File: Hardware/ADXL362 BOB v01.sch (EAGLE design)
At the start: 9 parts

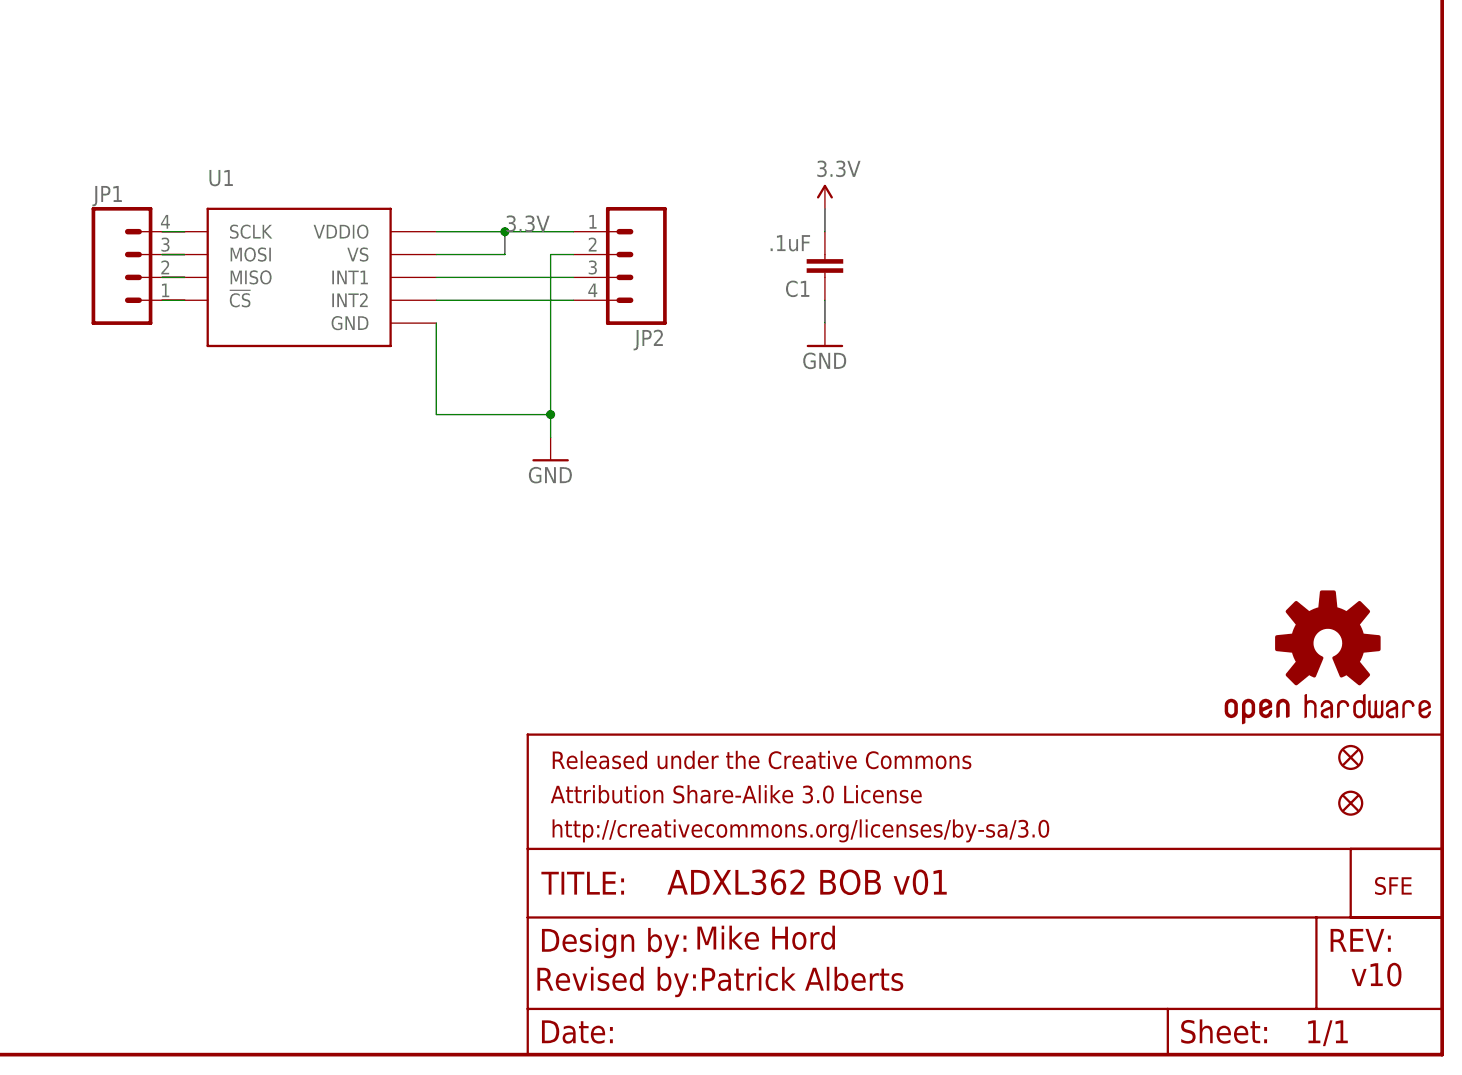
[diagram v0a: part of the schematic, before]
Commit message: Adding part info to README, adding current files to repo
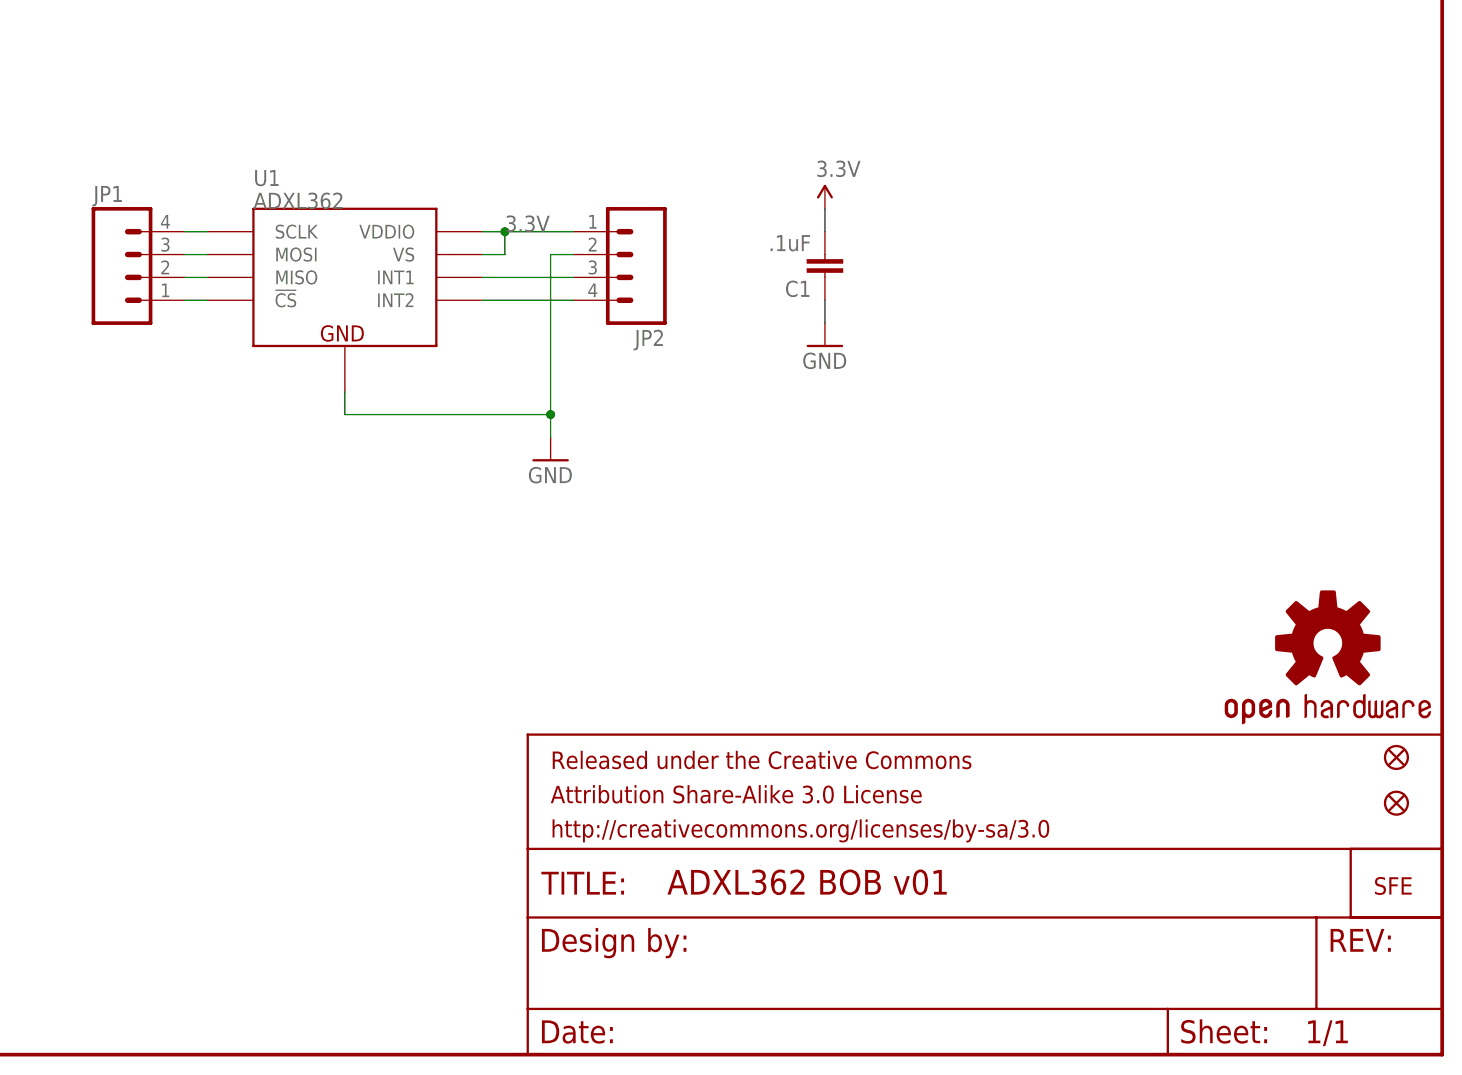
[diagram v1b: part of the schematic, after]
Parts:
- removed FID1, FID2: FIDUCIAL1X2, SparkFun-Aesthetics:FIDUCIAL1X2
- added JP4, JP5: FIDUCIALUFIDUCIAL, SparkFun:FIDUCIALUFIDUCIAL
- C1: device SparkFun-Capacitors:0.1UF-25V(+80/-20%)(0603) -> SparkFun-Passives:CAP0402-CAP
- U1: value (none) -> ADXL362; device SparkFun-Sensors:ADXL362ADXL362-1:1 -> SparkFun-Sensors:ADXL362
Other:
- note removed: "Mike Hord"
- note removed: "Revised by:Patrick Alberts"
- note removed: "v10"
- moved on the sheet: U1
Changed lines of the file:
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@@
 <?xml version="1.0" encoding="utf-8"?>
 <!DOCTYPE eagle SYSTEM "eagle.dtd">
-<eagle version="6.5.0">
+<eagle version="6.2">
 <drawing>
 <settings>
@@
 <layer number="106" name="bPlate" color="7" fill="1" visible="no" active="yes"/>
 <layer number="107" name="Crop" color="7" fill="1" visible="no" active="yes"/>
-<layer number="108" name="tplace-old" color="10" fill="1" visible="yes" active="yes"/>
-<layer number="109" name="ref-old" color="11" fill="1" visible="yes" active="yes"/>
 <layer number="116" name="Patch_BOT" color="9" fill="4" visible="no" active="yes"/>
 <layer number="121" name="_tsilk" color="7" fill="1" visible="no" active="yes"/>
@@
 <layer number="144" name="Drill_legend" color="7" fill="1" visible="no" active="yes"/>
 <layer number="151" name="HeatSink" color="7" fill="1" visible="no" active="yes"/>
-<layer number="199" name="Contour" color="7" fill="1" visible="yes" active="yes"/>
 <layer number="200" name="200bmp" color="1" fill="10" visible="no" active="yes"/>
 <layer number="201" name="201bmp" color="2" fill="10" visible="no" active="yes"/>
@@
 </classes>
 <parts>
-<part name="U1" library="SparkFun-Sensors" deviceset="ADXL362" device="ADXL362-1:1"/>
+<part name="U1" library="SparkFun-Sensors" deviceset="ADXL362" device=""/>
 <part name="JP1" library="SparkFun-Connectors" deviceset="M04" device="PTH"/>
 <part name="JP2" library="SparkFun-Connectors" deviceset="M04" device="PTH"/>
-<part name="C1" library="SparkFun-Capacitors" deviceset="0.1UF-25V(+80/-20%)(0603)" device="" value=".1uF">
+<part name="C1" library="SparkFun-Passives" deviceset="CAP" device="0402-CAP" value=".1uF">
 <attribute name="PROD_ID" value="CAP-00810"/>
 </part>
@@
 <part name="FRAME1" library="SparkFun-Aesthetics" deviceset="FRAME-LETTER" device=""/>
 <part name="GND2" library="SparkFun-Aesthetics" deviceset="GND" device=""/>
-<part name="FID1" library="SparkFun-Aesthetics" deviceset="FIDUCIAL" device="1X2"/>
-<part name="FID2" library="SparkFun-Aesthetics" deviceset="FIDUCIAL" device="1X2"/>
+<part name="JP4" library="SparkFun" deviceset="FIDUCIAL" device="UFIDUCIAL"/>
+<part name="JP5" library="SparkFun" deviceset="FIDUCIAL" device="UFIDUCIAL"/>
 </parts>
 <sheets>
 <sheet>
 <plain>
-<text x="238.76" y="7.62" size="2.54" layer="94">v10</text>
-<text x="165.862" y="11.684" size="2.54" layer="94">Mike Hord</text>
-<text x="148.082" y="7.112" size="2.54" layer="94">Revised by:Patrick Alberts</text>
 </plain>
 <instances>
-<instance part="U1" gate="G$1" x="121.92" y="86.36"/>
+<instance part="U1" gate="G$1" x="119.38" y="78.74"/>
 <instance part="JP1" gate="G$1" x="104.14" y="86.36"/>
 <instance part="JP2" gate="G$1" x="157.48" y="88.9" rot="R180"/>
@@
 <instance part="FRAME1" gate="G$2" x="147.32" y="0"/>
 <instance part="GND2" gate="1" x="149.86" y="66.04"/>
-<instance part="FID1" gate="G$1" x="238.76" y="33.02"/>
-<instance part="FID2" gate="G$1" x="238.76" y="27.94"/>
+<instance part="JP4" gate="G$1" x="243.84" y="33.02"/>
+<instance part="JP5" gate="G$1" x="243.84" y="27.94"/>
 </instances>
 <busses>
@@
 <pinref part="JP1" gate="G$1" pin="4"/>
 <pinref part="U1" gate="G$1" pin="SCLK"/>
-<wire x1="109.22" y1="91.44" x2="106.68" y2="91.44" width="0.1524" layer="91"/>
+<wire x1="109.22" y1="91.44" x2="111.76" y2="91.44" width="0.1524" layer="91"/>
 </segment>
 </net>
@@
 <pinref part="U1" gate="G$1" pin="MOSI"/>
 <pinref part="JP1" gate="G$1" pin="3"/>
-<wire x1="106.68" y1="88.9" x2="109.22" y2="88.9" width="0.1524" layer="91"/>
+<wire x1="111.76" y1="88.9" x2="109.22" y2="88.9" width="0.1524" layer="91"/>
 </segment>
 </net>
@@
 <pinref part="JP1" gate="G$1" pin="2"/>
 <pinref part="U1" gate="G$1" pin="MISO"/>
-<wire x1="109.22" y1="86.36" x2="106.68" y2="86.36" width="0.1524" layer="91"/>
+<wire x1="109.22" y1="86.36" x2="111.76" y2="86.36" width="0.1524" layer="91"/>
 </segment>
 </net>
@@
 <pinref part="U1" gate="G$1" pin="!CS"/>
 <pinref part="JP1" gate="G$1" pin="1"/>
-<wire x1="106.68" y1="83.82" x2="109.22" y2="83.82" width="0.1524" layer="91"/>
+<wire x1="111.76" y1="83.82" x2="109.22" y2="83.82" width="0.1524" layer="91"/>
 </segment>
 </net>
@@
 <wire x1="152.4" y1="91.44" x2="144.78" y2="91.44" width="0.1524" layer="91"/>
 <pinref part="U1" gate="G$1" pin="VS"/>
-<wire x1="144.78" y1="91.44" x2="137.16" y2="91.44" width="0.1524" layer="91"/>
-<wire x1="137.16" y1="88.9" x2="144.78" y2="88.9" width="0.1524" layer="91"/>
+<wire x1="144.78" y1="91.44" x2="142.24" y2="91.44" width="0.1524" layer="91"/>
+<wire x1="142.24" y1="88.9" x2="144.78" y2="88.9" width="0.1524" layer="91"/>
 <wire x1="144.78" y1="88.9" x2="144.78" y2="91.44" width="0.1524" layer="91"/>
 <junction x="144.78" y="91.44"/>
@@
 <pinref part="U1" gate="G$1" pin="INT1"/>
 <pinref part="JP2" gate="G$1" pin="3"/>
-<wire x1="152.4" y1="86.36" x2="137.16" y2="86.36" width="0.1524" layer="91"/>
+<wire x1="152.4" y1="86.36" x2="142.24" y2="86.36" width="0.1524" layer="91"/>
 </segment>
 </net>
@@
 <pinref part="U1" gate="G$1" pin="INT2"/>
 <pinref part="JP2" gate="G$1" pin="4"/>
-<wire x1="152.4" y1="83.82" x2="137.16" y2="83.82" width="0.1524" layer="91"/>
+<wire x1="152.4" y1="83.82" x2="142.24" y2="83.82" width="0.1524" layer="91"/>
 </segment>
 </net>
@@
 <segment>
 <pinref part="U1" gate="G$1" pin="GND"/>
-<wire x1="137.16" y1="81.28" x2="137.16" y2="71.12" width="0.1524" layer="91"/>
-<wire x1="137.16" y1="71.12" x2="149.86" y2="71.12" width="0.1524" layer="91"/>
+<wire x1="127" y1="73.66" x2="127" y2="71.12" width="0.1524" layer="91"/>
+<wire x1="127" y1="71.12" x2="149.86" y2="71.12" width="0.1524" layer="91"/>
 <wire x1="149.86" y1="71.12" x2="149.86" y2="88.9" width="0.1524" layer="91"/>
 <pinref part="JP2" gate="G$1" pin="2"/>
